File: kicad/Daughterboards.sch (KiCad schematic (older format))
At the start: 6 parts, among them P701 SLOT_A, P702 SLOT_D, P703 SLOT_B, P704 SLOT_E, P705 SLOT_C, P706 SLOT_F

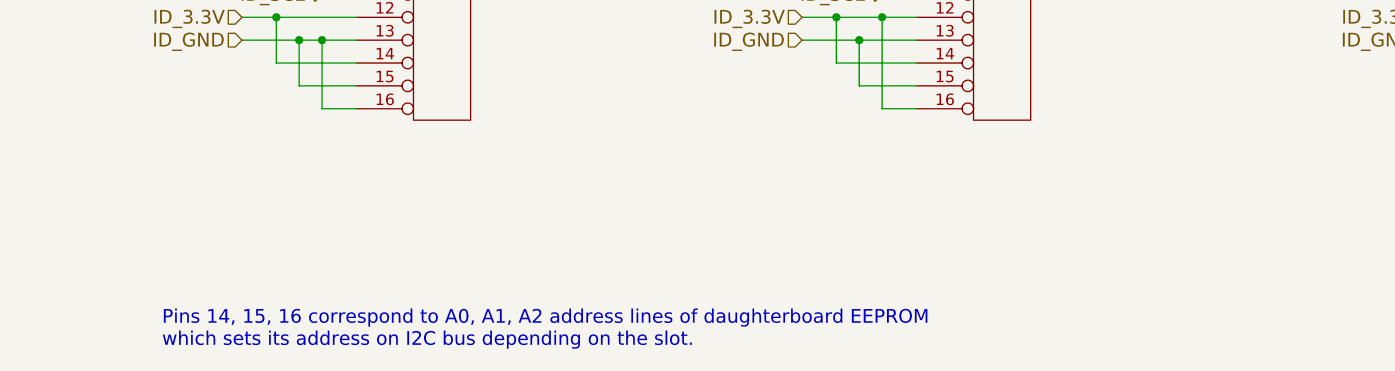
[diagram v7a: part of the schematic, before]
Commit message: Updated notes and sheet names
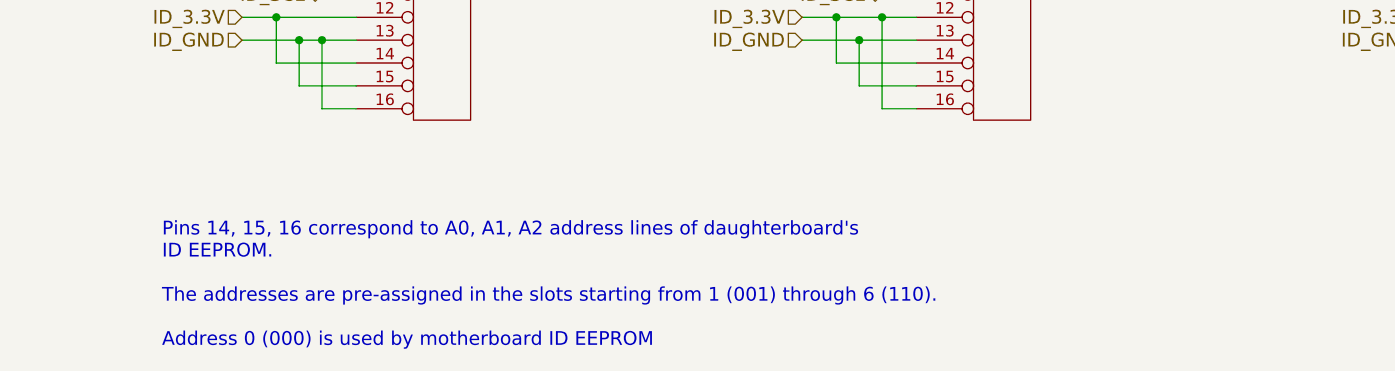
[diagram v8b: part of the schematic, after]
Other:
- note added: "Pins 14, 15, 16 correspond to A0, A1, A2 address lines of daughterboard's \nID EEPROM. \n\nThe addresses are pre-assigned in the slots starting from 1 (001) through 6 (110).\n\nAddress 0 (000) is used by motherboard ID EEPROM"
- note removed: "Pins 14, 15, 16 correspond to A0, A1, A2 address lines of daughterboard EEPROM \nwhich sets its address on I2C bus depending on the slot."
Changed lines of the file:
@@
 encoding utf-8
 Sheet 7 7
-Title ""
+Title "Daughterboard interface"
 Date "23 jun 2014"
 Rev ""
-Comp ""
+Comp "TimVideos"
 Comment1 ""
 Comment2 ""
@@
 Connection ~ 8450 5700
 Text Notes 2550 7050 0    60   ~ 0
-Pins 14, 15, 16 correspond to A0, A1, A2 address lines of daughterboard EEPROM \nwhich sets its address on I2C bus depending on the slot.
+Pins 14, 15, 16 correspond to A0, A1, A2 address lines of daughterboard's \nID EEPROM. \n\nThe addresses are pre-assigned in the slots starting from 1 (001) through 6 (110).\n\nAddress 0 (000) is used by motherboard ID EEPROM
 $EndSCHEMATC
